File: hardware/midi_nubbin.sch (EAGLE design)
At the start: 17 parts, among them IC1 PIC16F15345, SW1 6MMTACTSMT, SW2 6MMTACTSMT, SW3 6MMTACTSMT, SW45 6MMTACTSMT, SW5 6MMTACTSMT

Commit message: Change SSOP footprint
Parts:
- IC1: value PIC16F15345 -> PIC16F15345SSOP20; device jason_eagle6:PIC16F15345 -> jason_eagle6:PIC16F15345SSOP20
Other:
- note added: "***********TODO INCORRECT FOOTPRINT TO MCU 220R ON MIDI SIGNAL?"
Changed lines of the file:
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@@
 <part name="OUT" library="con-lumberg" deviceset="1503_02" device=""/>
 <part name="IN" library="con-lumberg" deviceset="1503_02" device=""/>
-<part name="IC1" library="jason_eagle6" deviceset="PIC16F15345" device=""/>
+<part name="IC1" library="jason_eagle6" deviceset="PIC16F15345" device="SSOP20" value="PIC16F15345SSOP20"/>
 <part name="SW5" library="jason_eagle6" deviceset="6MMTACTSMT" device=""/>
 <part name="SW45" library="jason_eagle6" deviceset="6MMTACTSMT" device=""/>
@@
 <text x="-17.526" y="157.734" size="1.778" layer="97">Ring (+5V)</text>
 <text x="-17.526" y="152.654" size="1.778" layer="97">Sleeve (GND)</text>
+<text x="-78.74" y="198.12" size="7.62" layer="91">***********TODO
+INCORRECT FOOTPRINT TO MCU
+220R ON MIDI SIGNAL?</text>
 </plain>
 <instances>
@@
 </schematic>
 </drawing>
+<compatibility>
+<note version="6.3" minversion="6.2.2" severity="warning">
+Since Version 6.2.2 text objects can contain more than one line,
+which will not be processed correctly with this version.
+</note>
+</compatibility>
 </eagle>

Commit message: BOARD V2
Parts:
- added R5: 220, rcl:R-EU_R0805
- added R6: (no value), rcl:R-EU_R0805
- R2: value 4k7 -> 220
- R3: value (none) -> 4k7
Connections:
- new net N$4: OUT.2, R5.1
- new net N$5: IN.2, R2.2
- net +5V: now also R4.2; no longer R2.2
- net LED2: now also R6.2; no longer R4.2
- net N$2: now also R6.1; no longer R4.1
- net N$3: now also R4.1; no longer R3.1
- net RX: now also R3.1; no longer IN.2
- net TX: now also R5.2; no longer OUT.2
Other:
- note added: "Aug 2022 - Sixty four pixels ltd"
- note added: "MIDI NUBBIN rev 2"
- note removed: "Apr 2022 - Sixty four pixels ltd"
- note removed: "MIDI NUBBIN rev 1"
- moved on the sheet: R2, R3, R4
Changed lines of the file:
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@@
 <part name="P+1" library="supply1" deviceset="+5V" device=""/>
 <part name="P+2" library="supply1" deviceset="+5V" device=""/>
-<part name="R2" library="rcl" deviceset="R-EU_" device="R0805" value="4k7"/>
+<part name="R3" library="rcl" deviceset="R-EU_" device="R0805" value="4k7"/>
 <part name="P+3" library="supply1" deviceset="+5V" device=""/>
 <part name="P+4" library="supply1" deviceset="+5V" device=""/>
@@
 <part name="GND6" library="supply1" deviceset="GND" device=""/>
 <part name="D2" library="adafruit" deviceset="LED" device="CHIPLED_0805"/>
-<part name="R4" library="rcl" deviceset="R-EU_" device="R0805"/>
+<part name="R6" library="rcl" deviceset="R-EU_" device="R0805"/>
 <part name="GND5" library="supply1" deviceset="GND" device=""/>
 <part name="C1" library="resistor" deviceset="CPOL-EU" device="SMCB"/>
@@
 <part name="SW1" library="jason_eagle6" deviceset="6MMTACTSMT" device=""/>
 <part name="SW2" library="jason_eagle6" deviceset="6MMTACTSMT" device=""/>
-<part name="R3" library="rcl" deviceset="R-EU_" device="R0805"/>
+<part name="R4" library="rcl" deviceset="R-EU_" device="R0805"/>
+<part name="R5" library="rcl" deviceset="R-EU_" device="R0805" value="220"/>
+<part name="R2" library="rcl" deviceset="R-EU_" device="R0805" value="220"/>
 </parts>
 <sheets>
 <sheet>
 <plain>
-<text x="-22.86" y="38.1" size="5.08" layer="97">MIDI NUBBIN rev 1</text>
-<text x="-22.86" y="30.48" size="5.08" layer="97">Apr 2022 - Sixty four pixels ltd</text>
+<text x="-22.86" y="38.1" size="5.08" layer="97">MIDI NUBBIN rev 2</text>
+<text x="-22.86" y="30.48" size="5.08" layer="97">Aug 2022 - Sixty four pixels ltd</text>
 <text x="-22.86" y="22.86" size="5.08" layer="97">CC-NC-BY-SA</text>
 <wire x1="-25.4" y1="45.72" x2="-25.4" y2="20.32" width="0.1524" layer="97"/>
@@
 <wire x1="88.9" y1="20.32" x2="88.9" y2="45.72" width="0.1524" layer="97"/>
 <wire x1="88.9" y1="45.72" x2="-25.4" y2="45.72" width="0.1524" layer="97"/>
-<text x="33.274" y="163.576" size="1.778" layer="97">Tip (Signal)</text>
+<text x="19.05" y="163.83" size="1.778" layer="97">Tip (Signal)</text>
 <text x="33.274" y="157.734" size="1.778" layer="97">Ring (+5V)</text>
 <text x="33.274" y="152.654" size="1.778" layer="97">Sleeve (GND)</text>
-<text x="-17.526" y="163.576" size="1.778" layer="97">Tip (Signal)</text>
+<text x="-5.842" y="163.576" size="1.778" layer="97">Tip (Signal)</text>
 <text x="-17.526" y="157.734" size="1.778" layer="97">Ring (+5V)</text>
 <text x="-17.526" y="152.654" size="1.778" layer="97">Sleeve (GND)</text>
@@
 <instance part="P+1" gate="1" x="48.26" y="182.88"/>
 <instance part="P+2" gate="1" x="-20.32" y="172.72"/>
-<instance part="R2" gate="G$1" x="7.62" y="147.32" smashed="yes" rot="R90">
+<instance part="R3" gate="G$1" x="7.62" y="147.32" smashed="yes" rot="R90">
 <attribute name="NAME" x="11.2014" y="148.59" size="1.778" layer="95" rot="R90"/>
 <attribute name="VALUE" x="10.922" y="143.51" size="1.778" layer="96" rot="R90"/>
@@
 <instance part="GND6" gate="1" x="-88.9" y="58.42"/>
 <instance part="D2" gate="G$1" x="-73.66" y="68.58"/>
-<instance part="R4" gate="G$1" x="-73.66" y="86.36" rot="R90"/>
+<instance part="R6" gate="G$1" x="-73.66" y="86.36" rot="R90"/>
 <instance part="GND5" gate="1" x="-73.66" y="58.42"/>
 <instance part="C1" gate="G$1" x="121.92" y="81.28"/>
@@
 <instance part="SW1" gate="G$1" x="7.62" y="73.66"/>
 <instance part="SW2" gate="G$1" x="7.62" y="60.96"/>
-<instance part="R3" gate="G$1" x="48.26" y="172.72" rot="R90"/>
+<instance part="R4" gate="G$1" x="48.26" y="172.72" rot="R90"/>
+<instance part="R5" gate="G$1" x="38.1" y="162.56" smashed="yes" rot="R180">
+<attribute name="NAME" x="35.814" y="165.8874" size="1.778" layer="95" rot="R180"/>
+<attribute name="VALUE" x="41.91" y="166.116" size="1.778" layer="96" rot="R180"/>
+</instance>
+<instance part="R2" gate="G$1" x="-10.16" y="162.56" smashed="yes" rot="R180">
+<attribute name="NAME" x="-12.446" y="165.8874" size="1.778" layer="95" rot="R180"/>
+<attribute name="VALUE" x="-6.35" y="166.116" size="1.778" layer="96" rot="R180"/>
+</instance>
 </instances>
 <busses>
@@
 <label x="30.48" y="139.7" size="1.778" layer="95"/>
 <wire x1="25.4" y1="162.56" x2="25.4" y2="139.7" width="0.1524" layer="91"/>
-<pinref part="OUT" gate="G$1" pin="2"/>
-<wire x1="55.88" y1="162.56" x2="25.4" y2="162.56" width="0.1524" layer="91"/>
+<pinref part="R5" gate="G$1" pin="2"/>
+<wire x1="33.02" y1="162.56" x2="25.4" y2="162.56" width="0.1524" layer="91"/>
 </segment>
 <segment>
@@
 <net name="RX" class="0">
 <segment>
-<pinref part="R2" gate="G$1" pin="1"/>
+<pinref part="R3" gate="G$1" pin="1"/>
 <wire x1="7.62" y1="142.24" x2="7.62" y2="139.7" width="0.1524" layer="91"/>
 <wire x1="7.62" y1="139.7" x2="2.54" y2="139.7" width="0.1524" layer="91"/>
@@
 <wire x1="2.54" y1="162.56" x2="2.54" y2="139.7" width="0.1524" layer="91"/>
 <junction x="2.54" y="139.7"/>
-<pinref part="IN" gate="G$1" pin="2"/>
-<wire x1="-25.4" y1="162.56" x2="2.54" y2="162.56" width="0.1524" layer="91"/>
+<pinref part="R2" gate="G$1" pin="1"/>
+<wire x1="-5.08" y1="162.56" x2="2.54" y2="162.56" width="0.1524" layer="91"/>
 </segment>
 <segment>
@@
 <net name="+5V" class="0">
 <segment>
-<pinref part="R2" gate="G$1" pin="2"/>
+<pinref part="R3" gate="G$1" pin="2"/>
 <pinref part="P+3" gate="1" pin="+5V"/>
 <wire x1="7.62" y1="152.4" x2="7.62" y2="170.18" width="0.1524" layer="91"/>
@@
 </segment>
 <segment>
-<pinref part="R3" gate="G$1" pin="2"/>
+<pinref part="R4" gate="G$1" pin="2"/>
 <pinref part="P+1" gate="1" pin="+5V"/>
 <wire x1="48.26" y1="177.8" x2="48.26" y2="180.34" width="0.1524" layer="91"/>
@@
 <label x="-53.34" y="106.68" size="1.778" layer="95"/>
 <wire x1="-73.66" y1="91.44" x2="-73.66" y2="106.68" width="0.1524" layer="91"/>
-<pinref part="R4" gate="G$1" pin="2"/>
+<pinref part="R6" gate="G$1" pin="2"/>
 </segment>
 <segment>
@@
 <net name="N$2" class="0">
 <segment>
-<pinref part="R4" gate="G$1" pin="1"/>
+<pinref part="R6" gate="G$1" pin="1"/>
 <pinref part="D2" gate="G$1" pin="A"/>
 <wire x1="-73.66" y1="81.28" x2="-73.66" y2="71.12" width="0.1524" layer="91"/>
@@
 <pinref part="OUT" gate="G$1" pin="3"/>
 <wire x1="48.26" y1="157.48" x2="55.88" y2="157.48" width="0.1524" layer="91"/>
-<pinref part="R3" gate="G$1" pin="1"/>
+<pinref part="R4" gate="G$1" pin="1"/>
 <wire x1="48.26" y1="157.48" x2="48.26" y2="167.64" width="0.1524" layer="91"/>
 </segment>
 </net>
+<net name="N$4" class="0">
+<segment>
+<pinref part="R5" gate="G$1" pin="1"/>
+<pinref part="OUT" gate="G$1" pin="2"/>
+<wire x1="43.18" y1="162.56" x2="55.88" y2="162.56" width="0.1524" layer="91"/>
+</segment>
+</net>
+<net name="N$5" class="0">
+<segment>
+<pinref part="IN" gate="G$1" pin="2"/>
+<pinref part="R2" gate="G$1" pin="2"/>
+<wire x1="-25.4" y1="162.56" x2="-15.24" y2="162.56" width="0.1524" layer="91"/>
+</segment>
+</net>

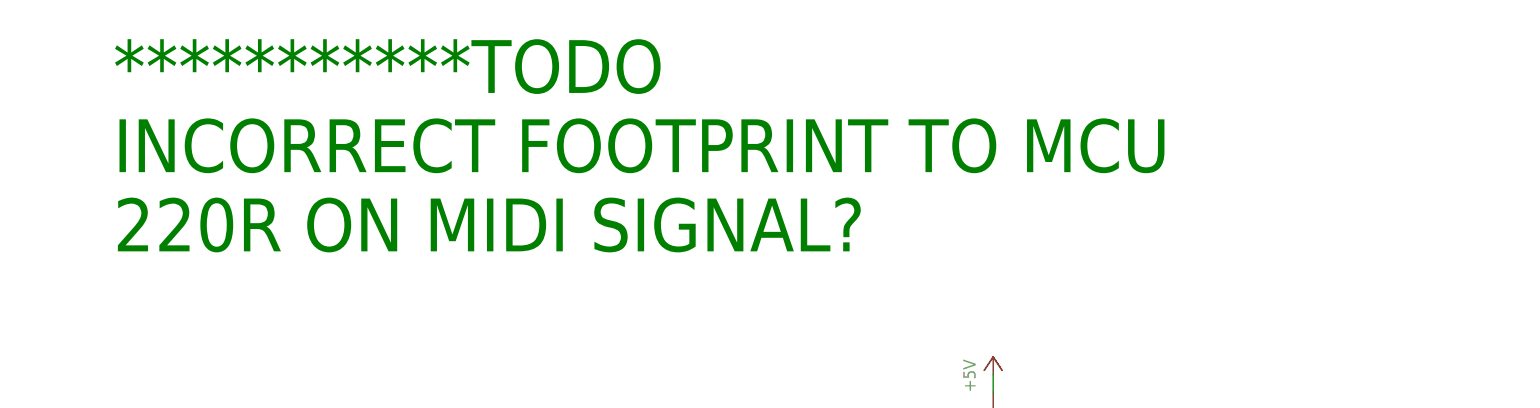
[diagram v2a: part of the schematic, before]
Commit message: mcu change
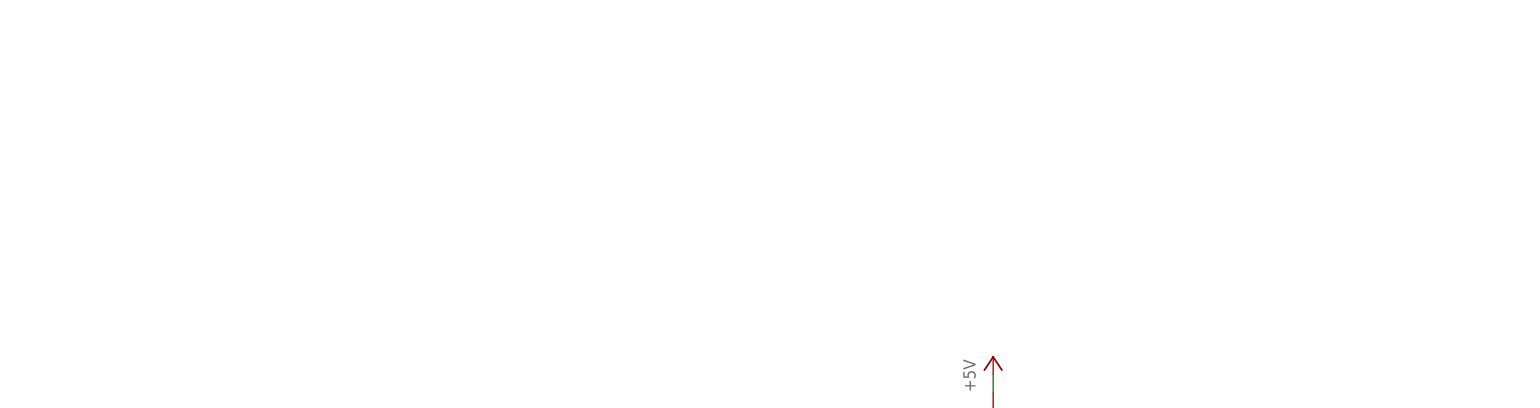
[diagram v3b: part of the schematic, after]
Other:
- note removed: "***********TODO INCORRECT FOOTPRINT TO MCU 220R ON MIDI SIGNAL?"
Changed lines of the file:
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@@
 <text x="-17.526" y="157.734" size="1.778" layer="97">Ring (+5V)</text>
 <text x="-17.526" y="152.654" size="1.778" layer="97">Sleeve (GND)</text>
-<text x="-78.74" y="198.12" size="7.62" layer="91">***********TODO
-INCORRECT FOOTPRINT TO MCU
-220R ON MIDI SIGNAL?</text>
 </plain>
 <instances>
@@
 </schematic>
 </drawing>
-<compatibility>
-<note version="6.3" minversion="6.2.2" severity="warning">
-Since Version 6.2.2 text objects can contain more than one line,
-which will not be processed correctly with this version.
-</note>
-</compatibility>
 </eagle>

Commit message: v3
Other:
- note added: "MIDI NUBBIN rev 3"
- note added: "Nov 2022 - Sixty four pixels ltd"
- note removed: "Aug 2022 - Sixty four pixels ltd"
- note removed: "MIDI NUBBIN rev 2"
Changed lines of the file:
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@@
 <sheet>
 <plain>
-<text x="-22.86" y="38.1" size="5.08" layer="97">MIDI NUBBIN rev 2</text>
-<text x="-22.86" y="30.48" size="5.08" layer="97">Aug 2022 - Sixty four pixels ltd</text>
+<text x="-22.86" y="38.1" size="5.08" layer="97">MIDI NUBBIN rev 3</text>
+<text x="-22.86" y="30.48" size="5.08" layer="97">Nov 2022 - Sixty four pixels ltd</text>
 <text x="-22.86" y="22.86" size="5.08" layer="97">CC-NC-BY-SA</text>
 <wire x1="-25.4" y1="45.72" x2="-25.4" y2="20.32" width="0.1524" layer="97"/>
